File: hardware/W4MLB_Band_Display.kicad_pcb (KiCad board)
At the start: 2 copper layers, 71 x 64 mm, 22 parts, among them J1 SSW-115-01-G-S, J2 SSW-115-01-G-S, J3 SSQ-108-01-T-D-LL, J4 SAMTEC-TST-108-01-X-D, J5 EJ503B, J6 796683-2, J7 PJRAN1X1U01X, J8 PJRAN1X1U01X, J9 Conn_01x10_Pin, U1 ESP32-DEVKIT-V1

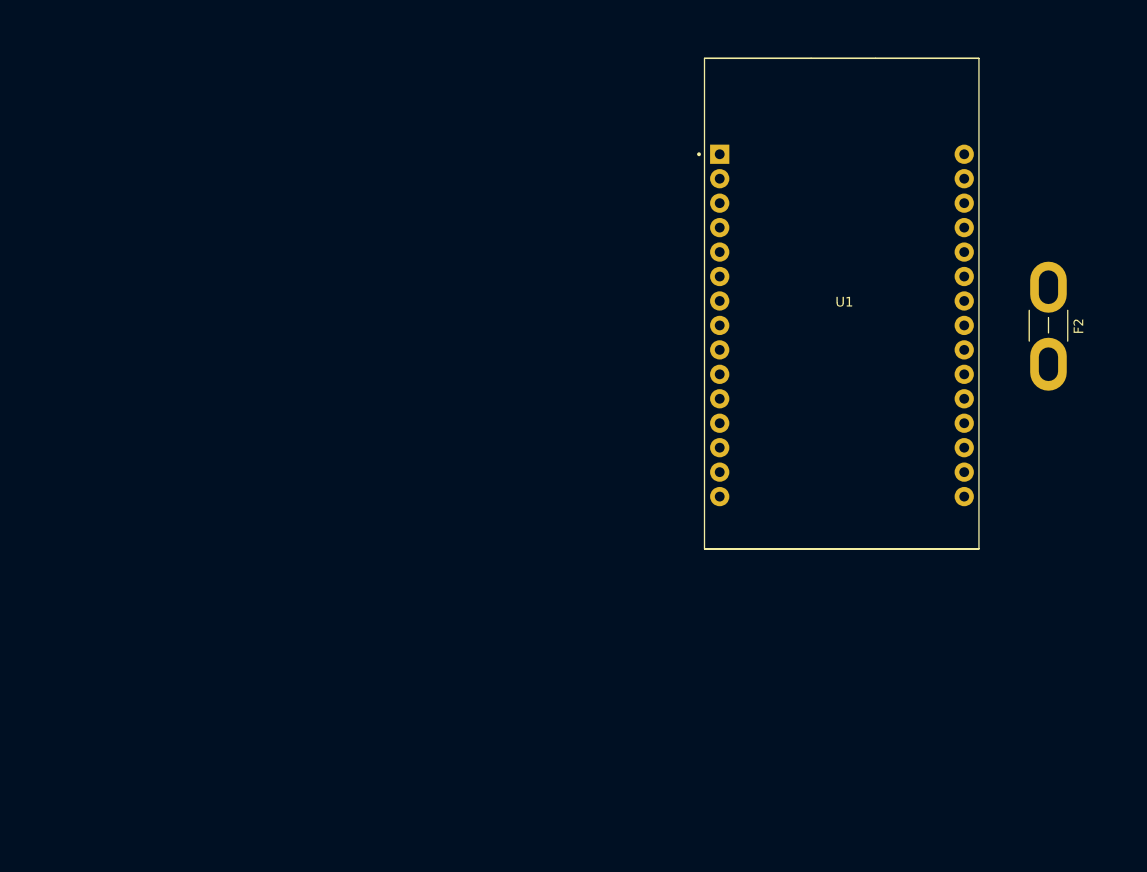
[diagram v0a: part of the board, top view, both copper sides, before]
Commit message: Added 3D model images.
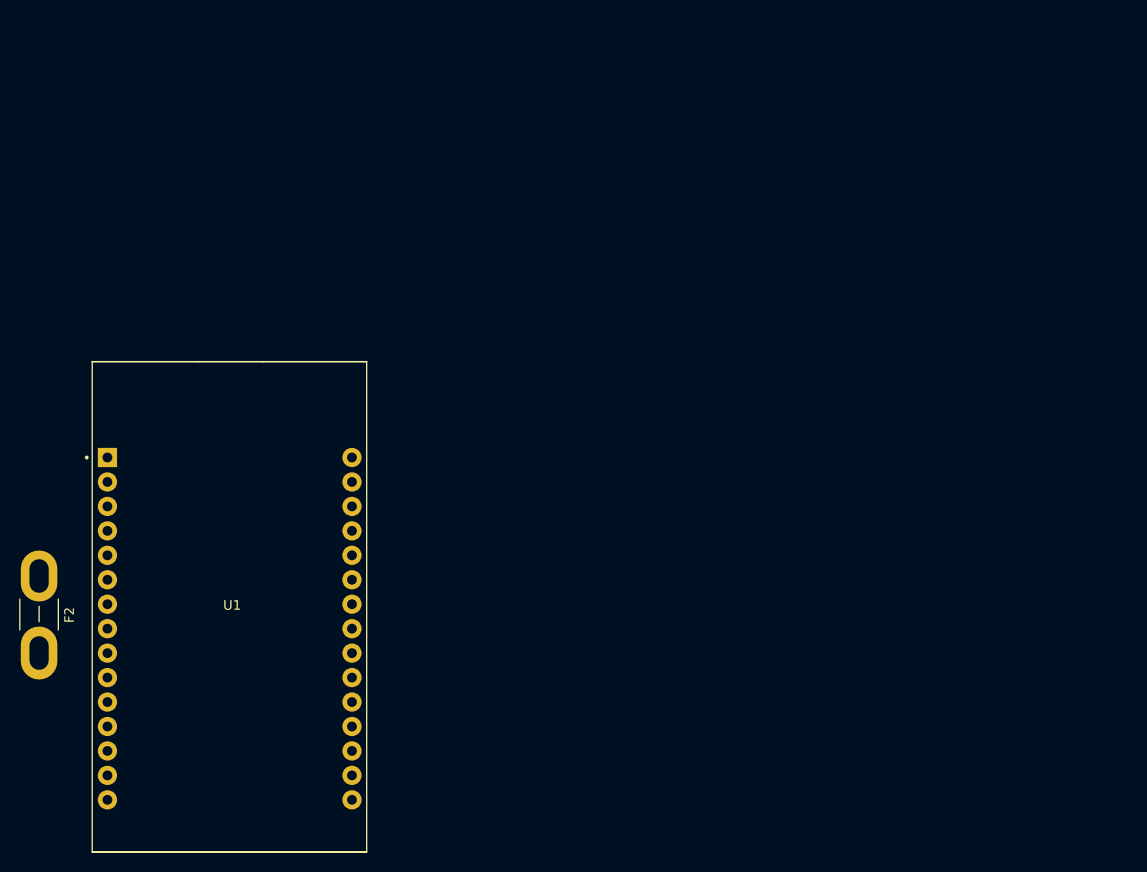
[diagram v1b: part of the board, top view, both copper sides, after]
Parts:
- moved F2 109.1 mm to (-48.9, 200.0)
- moved U1 71.0 mm to (-29.1, 195.2)
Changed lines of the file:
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@@
 	(footprint "Footprints:MODULE_ESP32_DEVKIT_V1"
 		(layer "F.Cu")
-		(at 34.55 163.705)
+		(at -29.05 195.205)
 		(property "Reference" "U1"
 			(at 0.25 -0.165 0)
@@
 			(polygon
 				(pts
-					(xy 25.64 182.69) (xy 43.33 182.69) (xy 43.33 189.18) (xy 25.64 189.18)
+					(xy -37.96 214.19) (xy -20.27 214.19) (xy -20.27 220.68) (xy -37.96 220.68)
 				)
 			)
@@
 			(polygon
 				(pts
-					(xy 25.64 182.69) (xy 43.33 182.69) (xy 43.33 189.18) (xy 25.64 189.18)
+					(xy -37.96 214.19) (xy -20.27 214.19) (xy -20.27 220.68) (xy -37.96 220.68)
 				)
 			)
@@
 			(polygon
 				(pts
-					(xy 25.64 182.69) (xy 43.33 182.69) (xy 43.33 189.18) (xy 25.64 189.18)
+					(xy -37.96 214.19) (xy -20.27 214.19) (xy -20.27 220.68) (xy -37.96 220.68)
 				)
 			)
@@
 	(footprint "Fuse:Fuse_Blade_Mini_directSolder"
 		(layer "F.Cu")
-		(at 56 170 90)
+		(at -48.85 200 90)
 		(descr "car blade fuse mini, direct solder")
 		(tags "car blade fuse mini")

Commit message: Screw terminal connector & Datasheets
Replaced LED Matric power connector with 2 position screw terminal for spade terminals. Also added datasheets for connector parts.
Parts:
- added Q1: MMBT2222A, Package_TO_SOT_SMD:SOT-23, F.Cu at (173.2, 75.2)
- added R2: 470, Resistor_SMD:R_0805_2012Metric_Pad1.20x1.40mm_HandSolder, F.Cu at (165.1, 74.3)
- J6: value 796683-2 -> 387206302; footprint Footprints:TE_796683-2 -> Footprints:CONN_SD-38720-002_02_MOL
- moved BZ1 8.06 mm to (186.5, 74.2), turned to 180 degrees
- moved J6 6.50 mm to (181.4, 97.5)
- moved F1 5.15 mm to (179.8, 107.8), turned to 180 degrees
- moved REF** 2.38 mm to (122.2, 66.5)
- moved REF** 0.85 mm to (187.0, 66.5)
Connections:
- BZ1 pad 1: GPIO19 -> +5V
- BZ1 pad 2: GND -> Net-(BZ1--)
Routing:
- net GPIO19: track 58.7 -> 44.6 mm
- net Net-(Q1-B): track 0.00 -> 6.23 mm
- net Net-(BZ1--): track 0.00 -> 5.66 mm
- net +5V: track 122.1 -> 119.9 mm
- net GND: track 2.12 -> 3.74 mm, vias 1 -> 2

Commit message: Moved Ref Docs & Corrected Buzzer pin
Moved Reference docs from /firmware/libs to Reference Docs at upper level.
Fixed issue where GPIO19 was connected to both TX and Buzzer. Moved buzzer to GPIO2
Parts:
- J9: value Conn_01x10_Pin -> Conn_01x09; footprint Connector_PinSocket_2.54mm:PinSocket_1x10_P2.54mm_Vertical -> Connector_PinHeader_2.54mm:PinHeader_1x09_P2.54mm_Vertical
- moved R2 2.77 mm to (167.7, 73.3)
- moved Q1 0.91 mm to (173.3, 74.3)
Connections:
- J9 pad 8: GPIO2 -> /+3.3VDC
- J9 pad 9: /+3.3VDC -> +5V
- R2 pad 1: GPIO19 -> GPIO2
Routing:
- net GPIO19: track 44.6 -> 23.5 mm
- net GPIO2: track 59.9 -> 48.8 mm, vias 0 -> 1
- net /+3.3VDC: track 58.3 -> 55.7 mm
- net +5V: track 119.9 -> 122.5 mm
- net Net-(Q1-B): track 6.23 -> 3.76 mm
- net GND: track 3.74 -> 4.70 mm
- net Net-(BZ1--): track 5.66 -> 5.13 mm
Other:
- board text removed: "GPIO2"

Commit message: Changed 10 pin connector to 9 pin
Modified 10 pin connector to 9 pins after assignment of GPIO2 to buzzer and it no longer being a spare pin.
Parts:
- J9: moved to F.Cu
- moved J9 0.11 mm to (152.5, 66.5), turned to 90 degrees

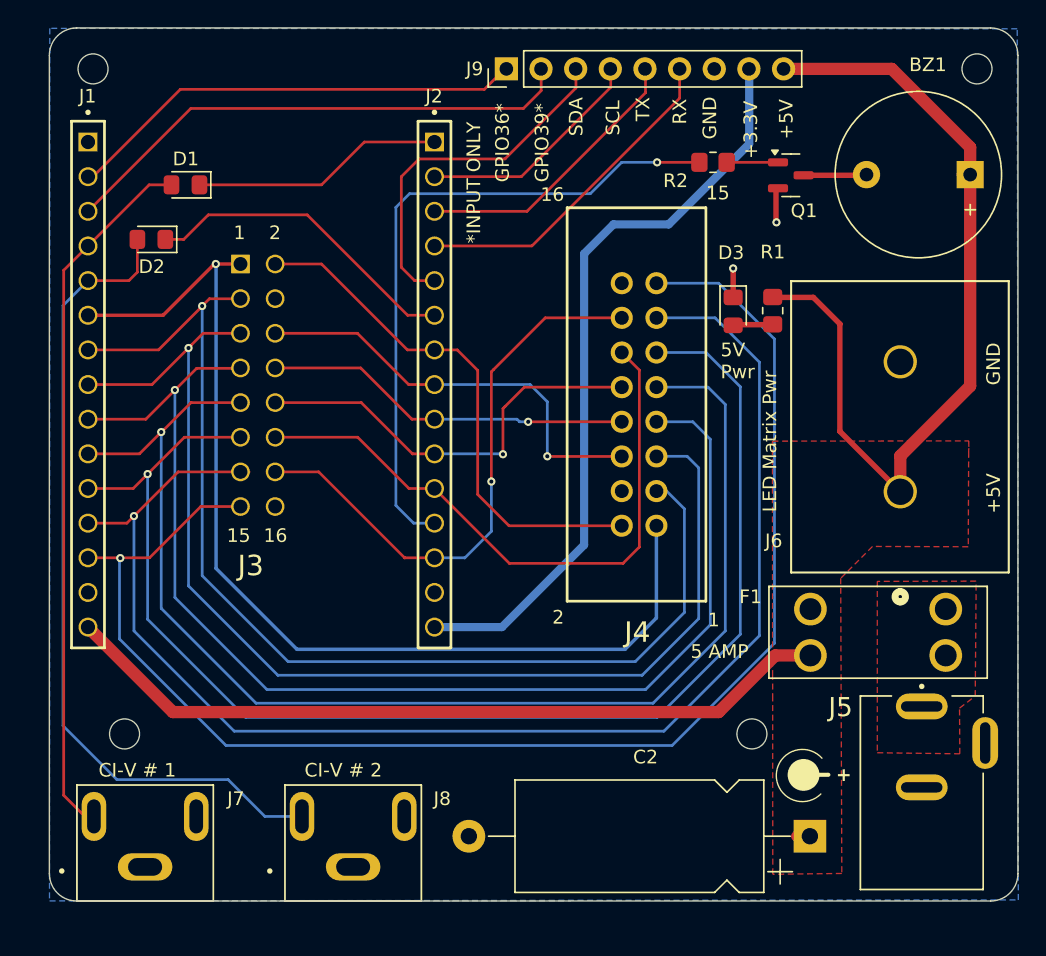
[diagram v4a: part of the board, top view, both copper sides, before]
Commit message: Smaller terminal block
Changed terminal block to smaller footprint.
Moved PCARS logo to front silkscreen.
Added RF bypass caps to CI-V inputs.
Adjusted location of D1 & D2.
Modified F1 footprint to allow pins 3 &4 to be connected.
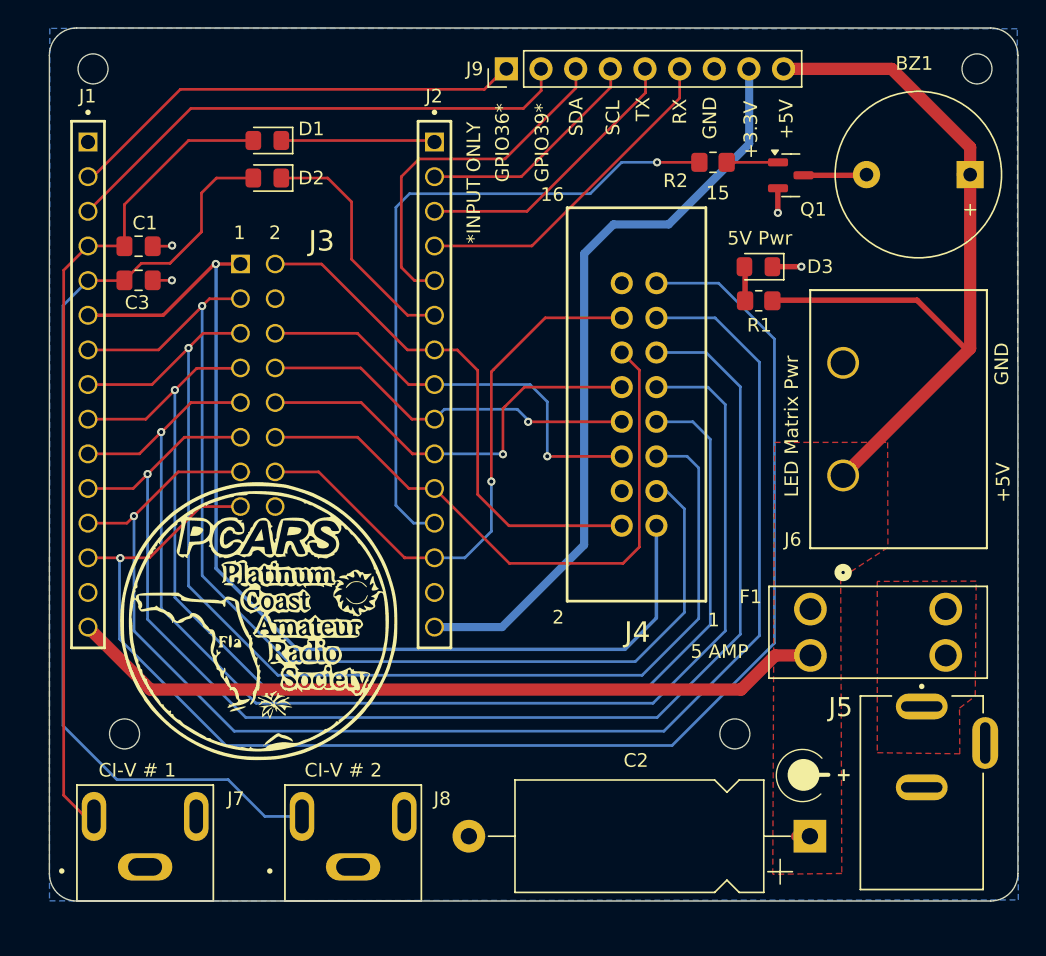
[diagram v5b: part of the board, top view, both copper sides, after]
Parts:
- removed REF**, REF04: MountingHole_2.2mm_M2, MountingHole:MountingHole_2.2mm_M2
- added C1: 0.005uF, Capacitor_SMD:C_0805_2012Metric_Pad1.18x1.45mm_HandSolder, F.Cu at (125.5, 79.5)
- added C3: 0.005uF, Capacitor_SMD:C_0805_2012Metric_Pad1.18x1.45mm_HandSolder, F.Cu at (125.5, 82.0)
- added MH2: MountingHole_2.2mm_M2, MountingHole:MountingHole_2.2mm_M2, F.Cu at (187.0, 66.5)
- added MH4: MountingHole_2.2mm_M2, MountingHole:MountingHole_2.2mm_M2, F.Cu at (169.2, 115.2)
- J6: value 387206302 -> 4DB-P108-02; footprint Footprints:CONN_SD-38720-002_02_MOL -> Footprints:CONN_4DB-P108-02_TEC
- moved D2 9.62 mm to (135.0, 74.5)
- moved D1 6.82 mm to (135.0, 71.8)
- moved J6 4.36 mm to (177.2, 96.3)
- moved D3 3.76 mm to (171.0, 81.0), turned to 180 degrees
- moved R1 1.26 mm to (171.0, 83.5), turned to 0 degrees
- renumbered REF** to MH1, REF** to MH3
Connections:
- F1 pad 3: (no net) -> /PWR IN
- F1 pad 4: (no net) -> +5V
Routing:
- net GPIO35: track 59.9 -> 70.7 mm
- net GPIO34: track 51.8 -> 61.0 mm
- net GPIO23: track 18.5 -> 11.3 mm
- net GPIO19: track 23.5 -> 17.9 mm
- net +5V: track 122.5 -> 117.4 mm
- net GND: track 4.70 -> 6.84 mm, vias 2 -> 4
- net GPIO17: track 27.0 -> 27.7 mm
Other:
- board text added: "PCARS Band Display Interface Board V1.0 https://github.com/danthepilotman/PCARS_Band_Display"

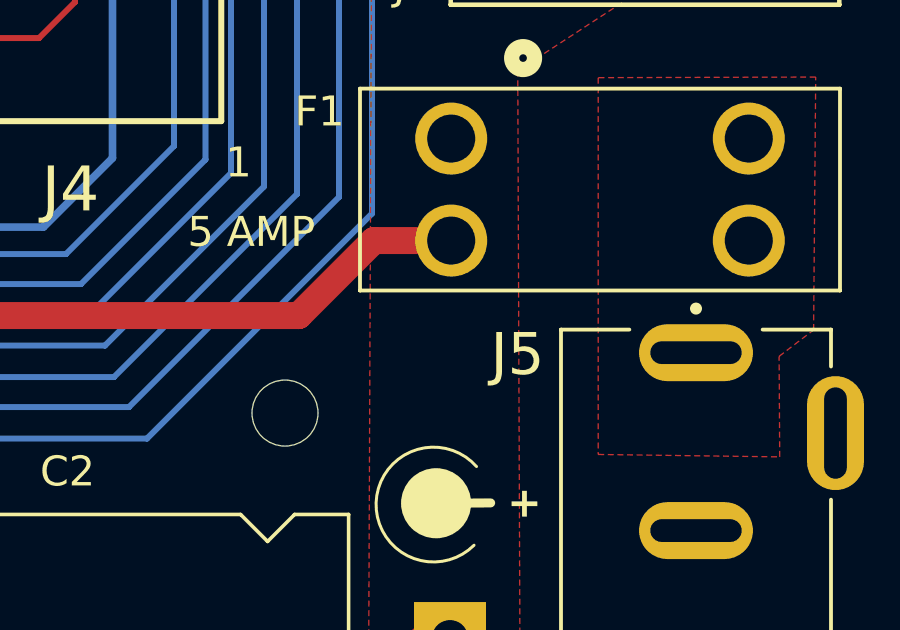
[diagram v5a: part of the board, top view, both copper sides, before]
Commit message: Added RF bypass cap to +5V DC supply input.
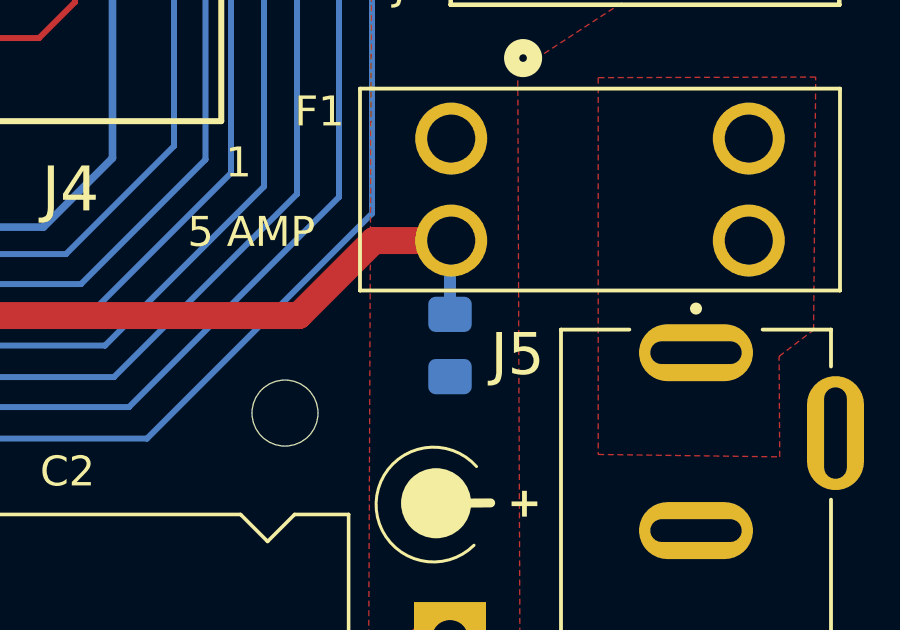
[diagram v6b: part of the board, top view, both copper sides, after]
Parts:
- added C4: 0.005uF, Capacitor_SMD:C_0805_2012Metric_Pad1.18x1.45mm_HandSolder, B.Cu at (174.8, 113.0)
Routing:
- net +5V: track 117.4 -> 119.9 mm
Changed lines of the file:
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@@
 		)
 	)
+	(footprint "Capacitor_SMD:C_0805_2012Metric_Pad1.18x1.45mm_HandSolder"
+		(layer "B.Cu")
+		(at 174.75 112.9975 -90)
+		(descr "Capacitor SMD 0805 (2012 Metric), square (rectangular) end terminal, IPC_7351 nominal with elongated pad for handsoldering. (Body size source: IPC-SM-782 page 76, https://www.pcb-3d.com/wordpress/wp-content/uploads/ipc-sm-782a_amendment_1_and_2.pdf, https://docs.google.com/spreadsheets/d/1BsfQQcO9C6DZCsRaXUlFlo91Tg2WpOkGARC1WS5S8t0/edit?usp=sharing), generated with kicad-footprint-generator")
+		(tags "capacitor handsolder")
+		(property "Reference" "C4"
+			(at 0 1.68 90)
+			(layer "B.SilkS")
+			(effects
+				(font
+					(size 1 1)
+					(thickness 0.15)
+				)
+				(justify mirror)
+			)
+		)
+		(property "Value" "0.005uF"
+			(at 0 -1.68 90)
+			(layer "B.Fab")
+			(effects
+				(font
+					(size 1 1)
+					(thickness 0.15)
+				)
+				(justify mirror)
+			)
+		)
+		(property "Datasheet" ""
+			(at 0 0 90)
+			(unlocked yes)
+			(layer "B.Fab")
+			(hide yes)
+			(effects
+				(font
+					(size 1.27 1.27)
+					(thickness 0.15)
+				)
+				(justify mirror)
+			)
+		)
+		(property "Description" "Unpolarized capacitor"
+			(at 0 0 90)
+			(unlocked yes)
+			(layer "B.Fab")
+			(hide yes)
+			(effects
+				(font
+					(size 1.27 1.27)
+					(thickness 0.15)
+				)
+				(justify mirror)
+			)
+		)
+		(property ki_fp_filters "C_*")
+		(sheetname "/")
+		(sheetfile "W4MLB_Band_Display.kicad_sch")
+		(attr smd)
+		(fp_line
+			(start -0.261252 0.735)
+			(end 0.261252 0.735)
+			(stroke
+				(width 0.12)
+				(type solid)
+			)
+			(layer "B.SilkS")
+		)
+		(fp_line
+			(start -0.261252 -0.735)
+			(end 0.261252 -0.735)
+			(stroke
+				(width 0.12)
+				(type solid)
+			)
+			(layer "B.SilkS")
+		)
+		(fp_line
+			(start -1.88 0.98)
+			(end 1.88 0.98)
+			(stroke
+				(width 0.05)
+				(type solid)
+			)
+			(layer "B.CrtYd")
+		)
+		(fp_line
+			(start 1.88 0.98)
+			(end 1.88 -0.98)
+			(stroke
+				(width 0.05)
+				(type solid)
+			)
+			(layer "B.CrtYd")
+		)
+		(fp_line
+			(start -1.88 -0.98)
+			(end -1.88 0.98)
+			(stroke
+				(width 0.05)
+				(type solid)
+			)
+			(layer "B.CrtYd")
+		)
+		(fp_line
+			(start 1.88 -0.98)
+			(end -1.88 -0.98)
+			(stroke
+				(width 0.05)
+				(type solid)
+			)
+			(layer "B.CrtYd")
+		)
+		(fp_line
+			(start -1 0.625)
+			(end 1 0.625)
+			(stroke
+				(width 0.1)
+				(type solid)
+			)
+			(layer "B.Fab")
+		)
+		(fp_line
+			(start 1 0.625)
+			(end 1 -0.625)
+			(stroke
+				(width 0.1)
+				(type solid)
+			)
+			(layer "B.Fab")
+		)
+		(fp_line
+			(start -1 -0.625)
+			(end -1 0.625)
+			(stroke
+				(width 0.1)
+				(type solid)
+			)
+			(layer "B.Fab")
+		)
+		(fp_line
+			(start 1 -0.625)
+			(end -1 -0.625)
+			(stroke
+				(width 0.1)
+				(type solid)
+			)
+			(layer "B.Fab")
+		)
+		(fp_text user "${REFERENCE}"
+			(at 0 0 90)
+			(layer "B.Fab")
+			(effects
+				(font
+					(size 0.5 0.5)
+					(thickness 0.08)
+				)
+				(justify mirror)
+			)
+		)
+		(pad "1" smd roundrect
+			(at -1.0375 0 270)
+			(size 1.175 1.45)
+			(layers "B.Cu" "B.Mask" "B.Paste")
+			(roundrect_rratio 0.212766)
+			(net 2 "+5V")
+			(pintype "passive")
+		)
+		(pad "2" smd roundrect
+			(at 1.0375 0 270)
+			(size 1.175 1.45)
+			(layers "B.Cu" "B.Mask" "B.Paste")
+			(roundrect_rratio 0.212766)
+			(net 1 "GND")
+			(pintype "passive")
+		)
+		(embedded_fonts no)
+		(model "${KICAD9_3DMODEL_DIR}/Capacitor_SMD.3dshapes/C_0805_2012Metric.wrl"
+			(offset
+				(xyz 0 0 0)
+			)
+			(scale
+				(xyz 1 1 1)
+			)
+			(rotate
+				(xyz 0 0 0)
+			)
+		)
+	)
 	(footprint "Footprints:SAMTEC_SSQ-108-01-T-D-LL"
 		(locked yes)
@@
 		(net 2)
 	)
+	(segment
+		(start 174.75 111.96)
+		(end 174.75 109.54)
+		(width 0.4)
+		(layer "B.Cu")
+		(net 2)
+	)
+	(segment
+		(start 174.71 111.92)
+		(end 174.75 111.96)
+		(width 0.2)
+		(layer "B.Cu")
+		(net 2)
+	)
+	(segment
+		(start 174.75 109.54)
+		(end 174.79 109.5)
+		(width 0.2)
+		(layer "B.Cu")
+		(net 2)
+	)
